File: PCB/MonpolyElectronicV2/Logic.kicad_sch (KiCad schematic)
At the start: 41 parts, among them J1 Conn_01x14, J3 2171820001, J4 Conn_01x05, J5 Conn_01x04, J6 Conn_01x10, J7 Conn_01x05, Q1 NPN, Q2 NPN, SW1 SW_Push, SW2 SW_Push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

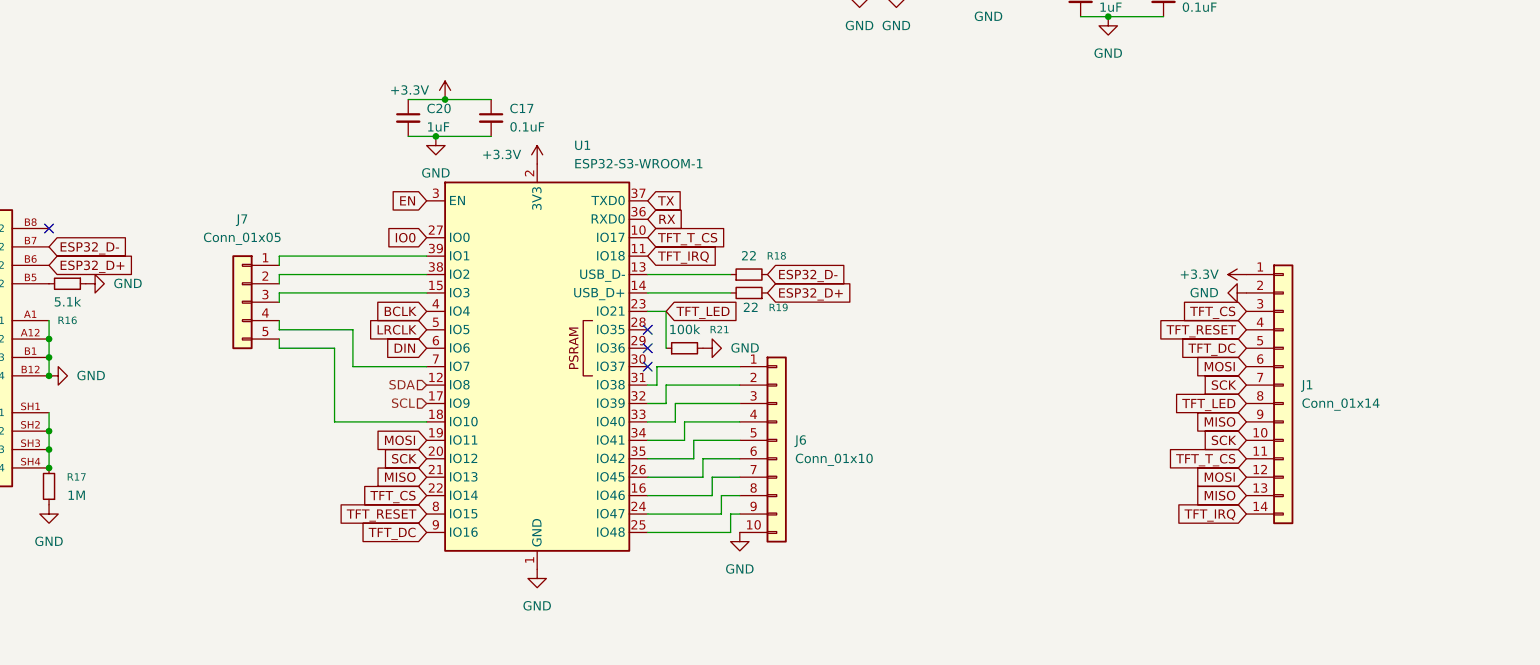
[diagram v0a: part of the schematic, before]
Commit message: assign footprints + multiple backlight options
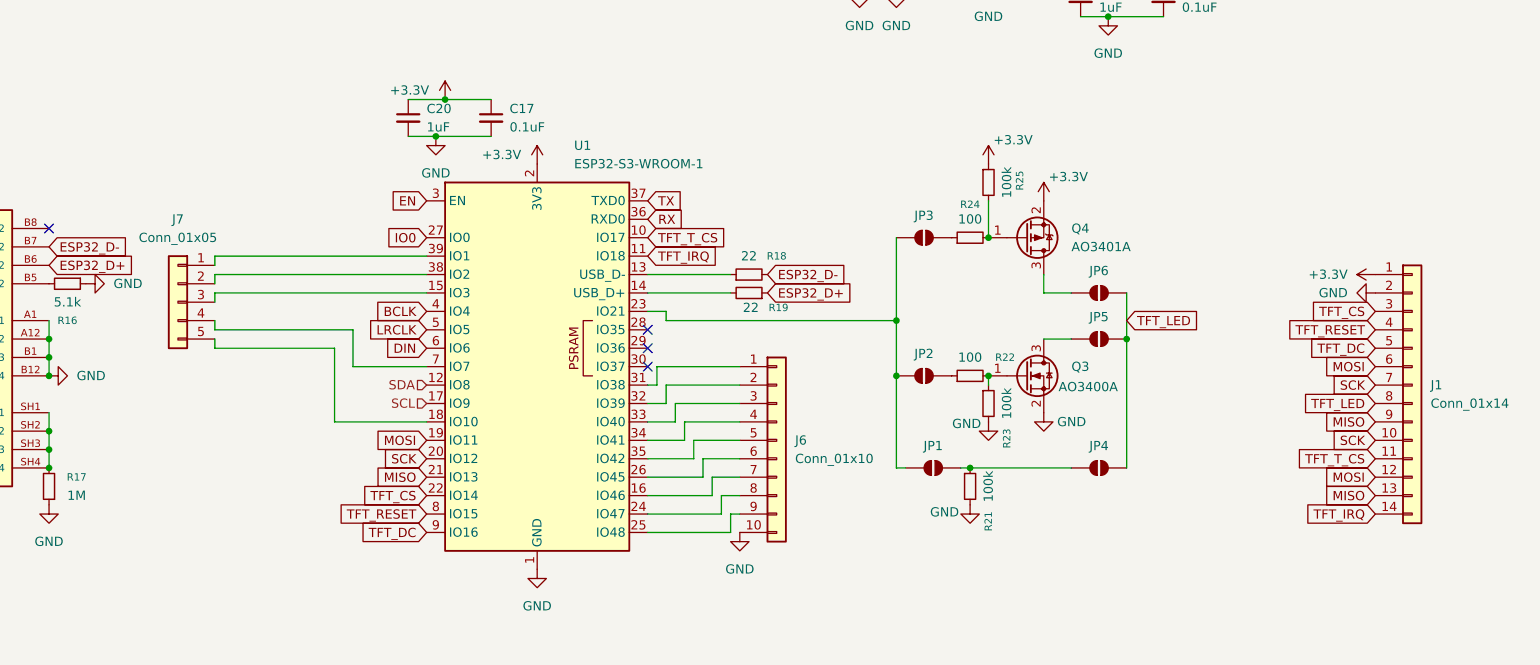
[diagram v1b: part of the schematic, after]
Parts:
- added JP1, JP2, JP3, JP4, JP5, JP6: SolderJumper_2_Open, Jumper:SolderJumper-2_P1.3mm_Open_TrianglePad1.0x1.5mm, symbol Jumper:SolderJumper_2_Open
- added Q3: AO3400A, Package_TO_SOT_SMD:SOT-23, symbol Transistor_FET:AO3400A
- added Q4: AO3401A, Package_TO_SOT_SMD:SOT-23, symbol Transistor_FET:AO3401A
- added R22, R24: 100, Resistor_SMD:R_0603_1608Metric, symbol Device:R_Small
- added R23, R25: 100k, Resistor_SMD:R_0603_1608Metric, symbol Device:R_Small
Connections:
- net +3.3V: now also Q4.2 (S), R25.1
- net GND: now also Q3.2 (S), R23.2
- net TFT_LED: now also JP4.1 (A), JP5.1 (A), JP6.1 (A); no longer R21.1, U1.23 (IO21)
- new net: JP5.2 (B), Q3.3 (D)
- new net: JP1.2 (B), JP2.2 (B), JP3.2 (B), U1.23 (IO21)
- new net: JP1.1 (A), JP4.2 (B), R21.1
- new net: Q3.1 (G), R22.2, R23.1
- new net: JP3.1 (A), R24.1
- new net: Q4.1 (G), R24.2, R25.2
- new net: JP6.2 (B), Q4.3 (D)
- new net: JP2.1 (A), R22.1
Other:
- moved on the sheet: J1, J7, R21

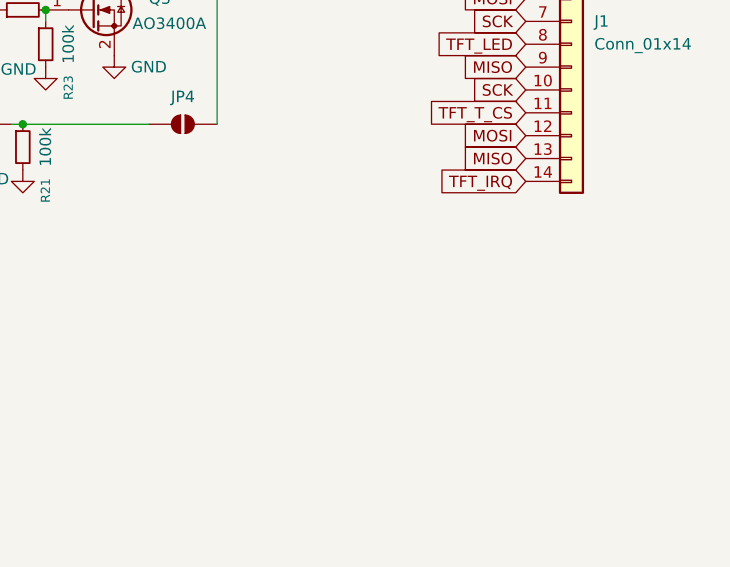
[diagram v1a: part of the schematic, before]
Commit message: add decoupling caps to TFT B_LED
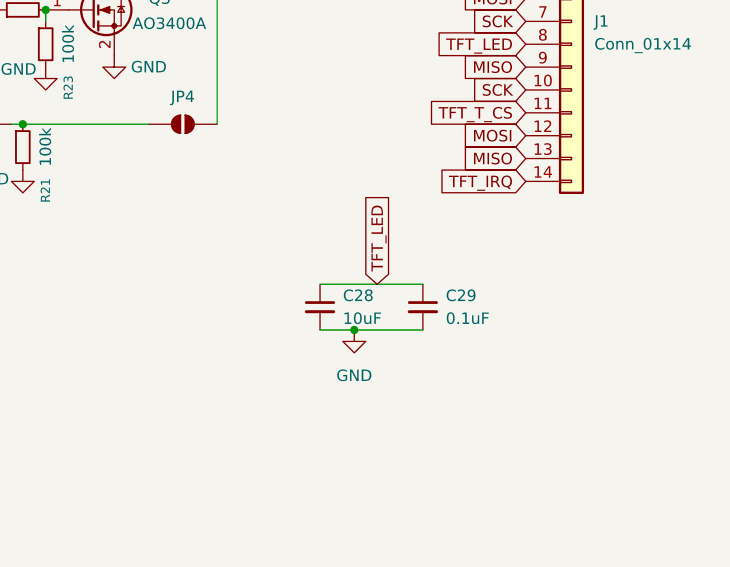
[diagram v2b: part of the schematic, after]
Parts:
- added C28: 10uF, Capacitor_SMD:C_0603_1608Metric, symbol Device:C_Small
- added C29: 0.1uF, Capacitor_SMD:C_0603_1608Metric, symbol Device:C_Small
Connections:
- net GND: now also C28.2, C29.2
- net TFT_LED: now also C28.1, C29.1
